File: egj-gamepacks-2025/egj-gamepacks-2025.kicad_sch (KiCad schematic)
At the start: 54 parts, among them J1 USB_B_Micro, J3 SM03B-SRSS-TB, J5 GameBoy_GamePak_AGB-002, SW1 SW_Push, SW2 SW_Push, U1 W25Q128JVS, U10 SP3012-06UTG, U2 DNF, U3 NCP1117-3.3_SOT223, U4 RP2350_80QFN, U5 USBLC6-2P6, U6 SP3012-06UTG, U7 SP3012-06UTG, U8 SP3012-06UTG, U9 SP3012-06UTG, Y1 ABM8-272-T3

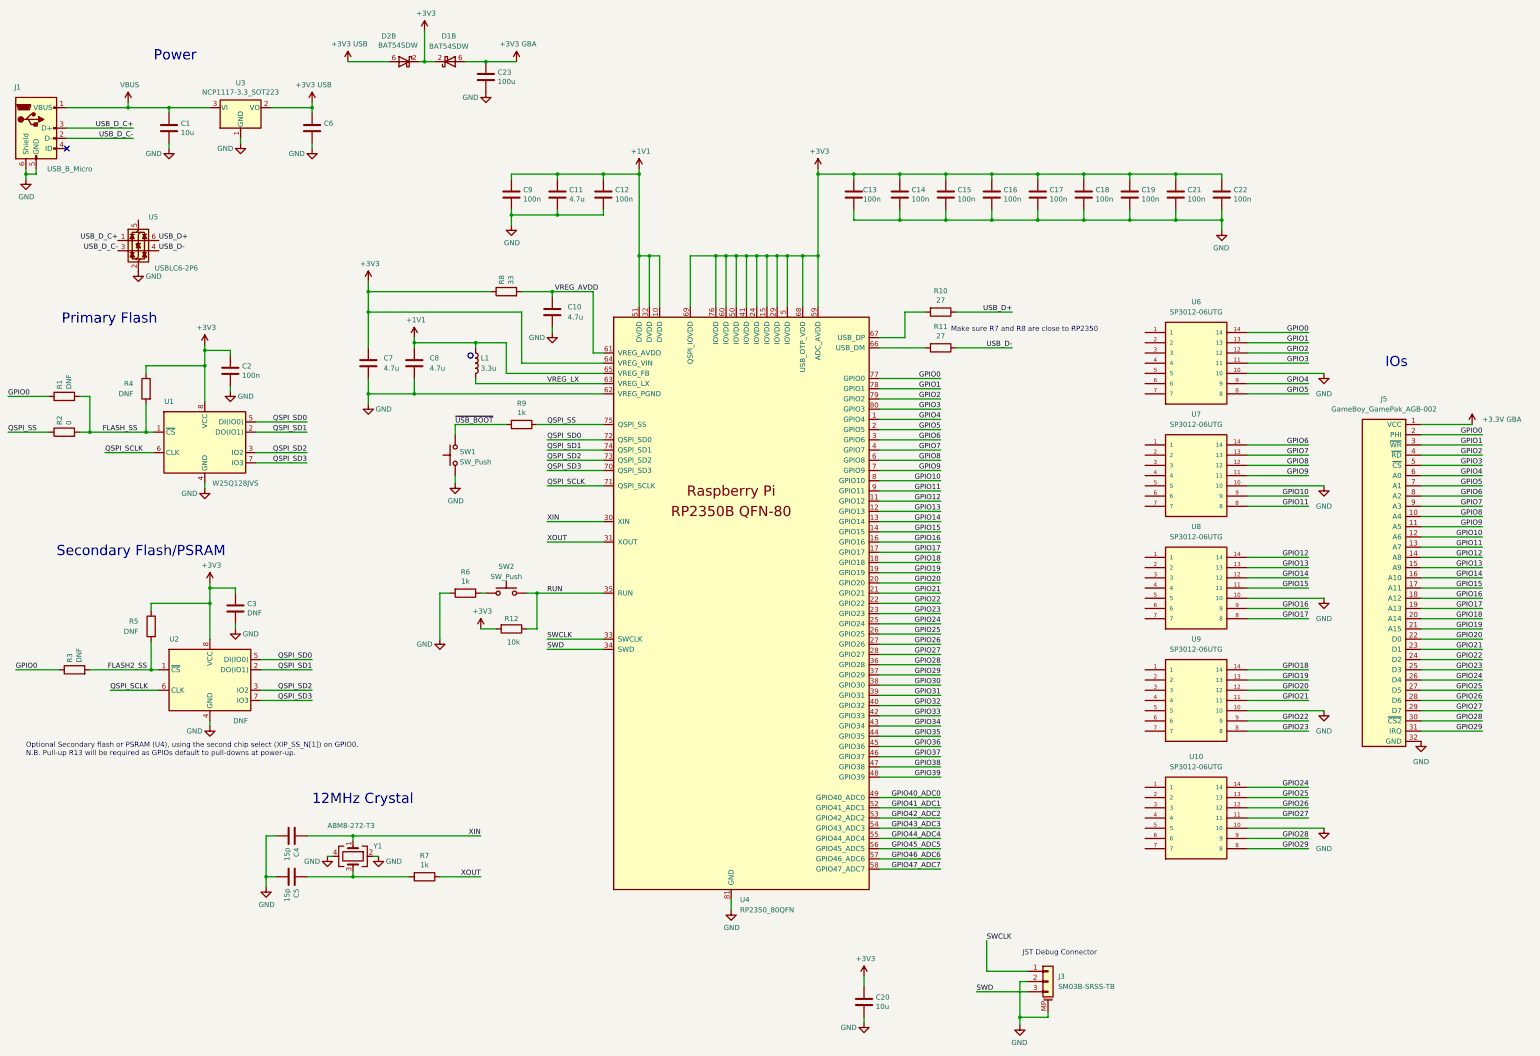
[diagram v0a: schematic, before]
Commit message: add new schemas
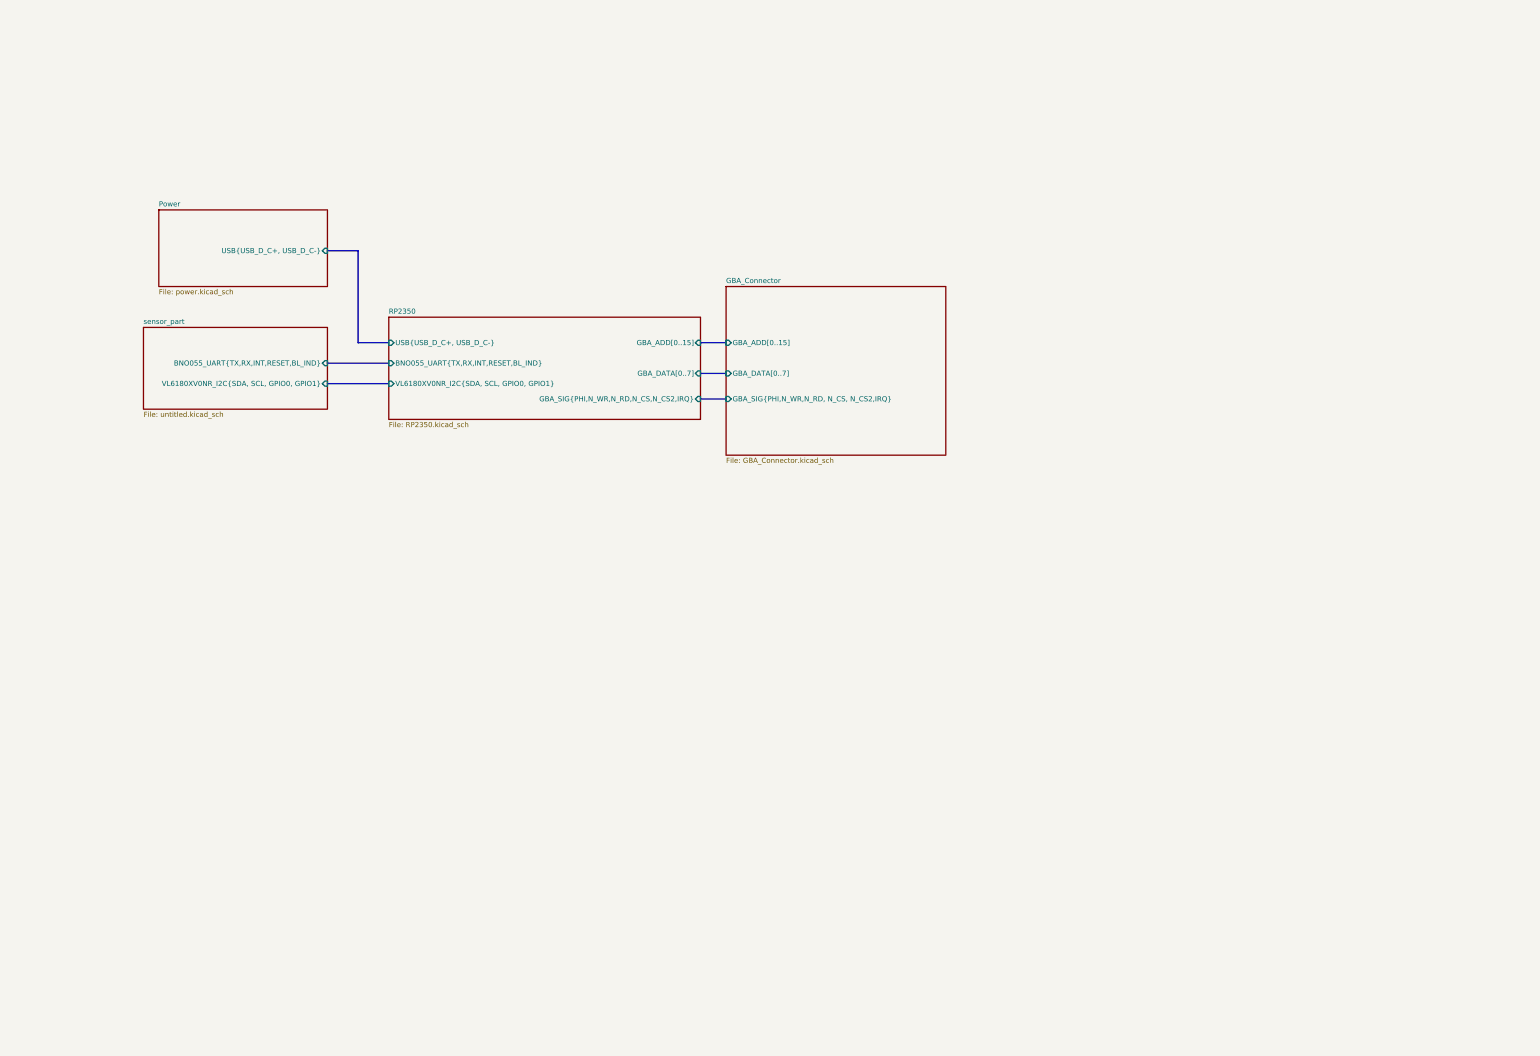
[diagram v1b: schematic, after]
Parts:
- removed C1, C20, C6: 10u, Capacitor_SMD:C_0805_2012Metric, symbol Device:C
- removed C10, C11: 4.7u, Capacitor_SMD:C_0402_1005Metric, symbol Device:C
- removed C12, C13, C14, C15, C16, C17, C18, C19, C2, C21, C22, C9: 100n, Capacitor_SMD:C_0402_1005Metric, symbol Device:C
- removed C23: 100u, Capacitor_SMD:C_0805_2012Metric, symbol Device:C
- removed C3: DNF, Capacitor_SMD:C_0402_1005Metric, symbol Device:C
- removed C4, C5: 15p, Capacitor_SMD:C_0402_1005Metric, symbol Device:C
- removed C7, C8: 4.7u, RP2350_80QFN_minimal:C_0402_1005Metric_small_pads, symbol Device:C
- removed D1, D2: BAT54SDW, Package_TO_SOT_SMD:SOT-363_SC-70-6, symbol Diode:BAT54SDW
- removed J1: USB_B_Micro, Connector_USB:USB_Micro-B_Amphenol_10103594-0001LF_Horizontal, symbol Connector:USB_B_Micro
- removed J3: SM03B-SRSS-TB, Connector_JST:JST_SH_SM03B-SRSS-TB_1x03-1MP_P1.00mm_Horizontal, symbol Connector_Generic_MountingPin:Conn_01x03_MountingPin
- removed J5: GameBoy_GamePak_AGB-002, Connector_GameBoy:GameBoy_GamePak_AGB-002_P1.50mm_Edge, symbol Connector_GameBoy:GameBoy_GamePak_AGB-002
- removed L1: 3.3u, RP2350_80QFN_minimal:L_pol_2016, symbol Device:L
- removed R1, R3, R4, R5: DNF, Resistor_SMD:R_0402_1005Metric, symbol Device:R
- removed R10, R11: 27, Resistor_SMD:R_0402_1005Metric, symbol Device:R
- removed R12: 10k, Resistor_SMD:R_0402_1005Metric, symbol Device:R
- removed R2: 0, Resistor_SMD:R_0402_1005Metric, symbol Device:R
- removed R6, R7, R9: 1k, Resistor_SMD:R_0402_1005Metric, symbol Device:R
- removed R8: 33, Resistor_SMD:R_0402_1005Metric, symbol Device:R
- removed SW1, SW2: SW_Push, Button_Switch_SMD:SW_Push_1P1T_NO_Vertical_Wuerth_434133025816, symbol Switch:SW_Push
- removed U1: W25Q128JVS, Package_SO:SOIC-8_5.23x5.23mm_P1.27mm, symbol Memory_Flash:W25Q128JVS
- removed U10, U6, U7, U8, U9: SP3012-06UTG, SP3012-06UTG:SON50P350X135X55-14N, symbol SP3012-06UTG:SP3012-06UTG
- removed U2: DNF, Package_SO:SOIC-8_5.23x5.23mm_P1.27mm, symbol Memory_Flash:W25Q128JVS
- removed U3: NCP1117-3.3_SOT223, Package_TO_SOT_SMD:SOT-223-3_TabPin2, symbol Regulator_Linear:NCP1117-3.3_SOT223
- removed U4: RP2350_80QFN, RP2350_80QFN_minimal:RP2350-QFN-80-1EP_10x10_P0.4mm_EP3.4x3.4mm_ThermalVias, symbol MCU_RaspberryPi_RP2350:RP2350_80QFN
- removed U5: USBLC6-2P6, Package_TO_SOT_SMD:SOT-666, symbol Power_Protection:USBLC6-2P6
- removed Y1: ABM8-272-T3, Crystal:Crystal_SMD_3225-4Pin_3.2x2.5mm, symbol Device:Crystal_GND24
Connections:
- no-connect marks 1 -> 0
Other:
- added sheet GBA_Connector (GBA_Connector.kicad_sch)
- added sheet Power (power.kicad_sch)
- added sheet RP2350 (RP2350.kicad_sch)
- added sheet sensor_part (untitled.kicad_sch)
- note removed: "12MHz Crystal"
- note removed: "IOs"
- note removed: "JST Debug Connector"
- note removed: "Make sure R7 and R8 are close to RP2350"
- note removed: "Optional Secondary flash or PSRAM (U4), using the second chip select (XIP_SS_N[1]) on GPIO0. N.B. Pull-up R13 will be required as GPIOs default to pull-downs at power-up."
- note removed: "Power"
- note removed: "Primary Flash"
- note removed: "Secondary Flash/PSRAM"
